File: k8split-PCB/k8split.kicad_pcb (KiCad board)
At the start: 2 copper layers, 397.3 x 124 mm, 243 parts, among them J1 AVR-ISP-6, J2 AVR-ISP-6, J3 Breakaway_Tabs, J4 Breakaway_Tabs, J5 Breakaway_Tabs, J6 Breakaway_Tabs, J7 Breakaway_Tabs, J8 Breakaway_Tabs, J9 Breakaway_Tabs, SW1 SW_Push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

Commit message: redid some silkscreen, cleaned up button move
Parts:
- removed the G*** at (257.6, 84.8)
- removed the G*** at (-2.54, 85.3)
- added G***: LOGO, cad:l, F.Cu at (119.9, 116.3)
- added G***: LOGO, cad:r, F.Cu at (158.5, 78.7)
- moved SW2 2.22 mm to (159.0, 77.2)
- moved J2 2.22 mm to (159.0, 69.6)
- moved R2 1.02 mm to (163.6, 71.1)
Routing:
- net SCK-R: track 119.8 -> 122.2 mm
- net RESET-R: track 107.7 -> 109.4 mm
- net MOSI-R: track 120.4 -> 121.4 mm
- net +5VA: track 339.9 -> 340.7 mm
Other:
- outline, holes or cut-outs redrawn

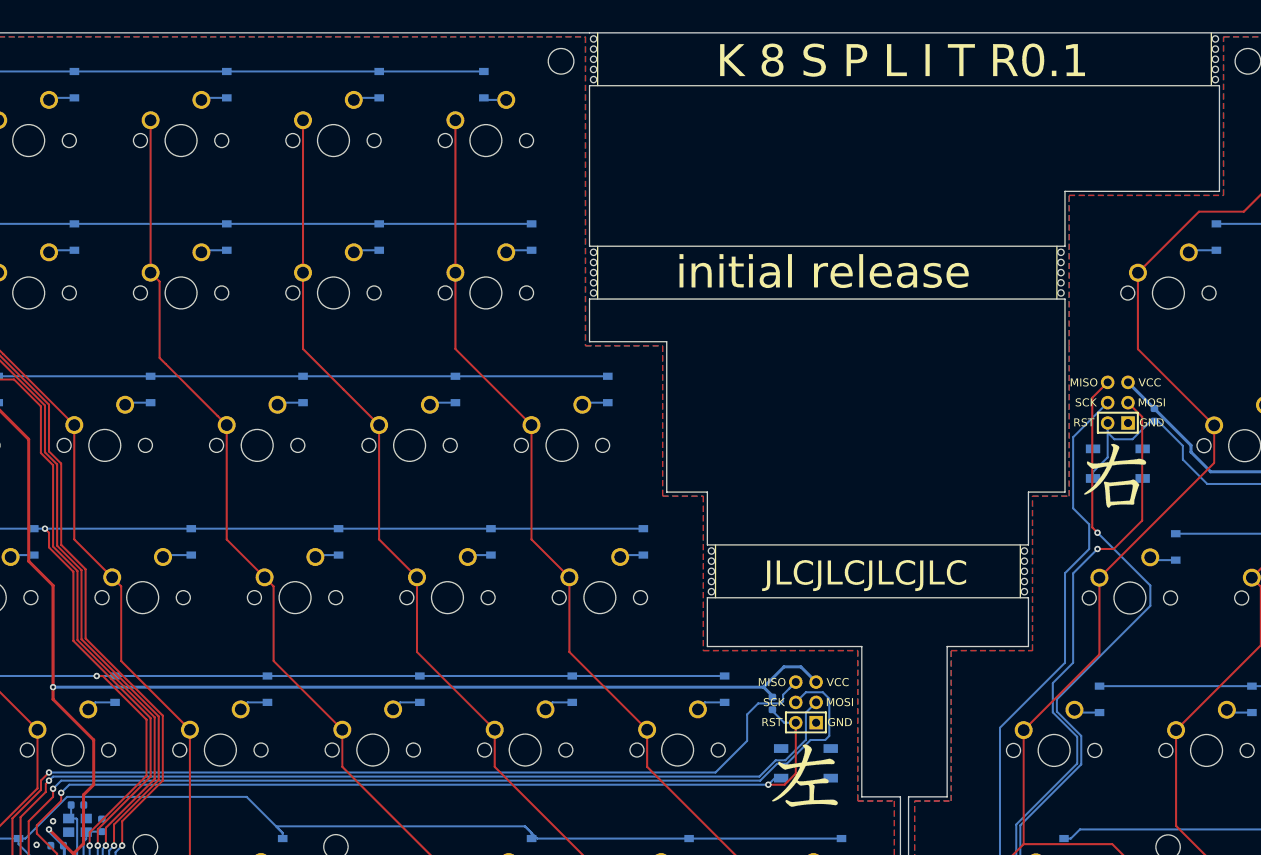
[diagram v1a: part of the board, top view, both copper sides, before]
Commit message: move silk on avr connectors
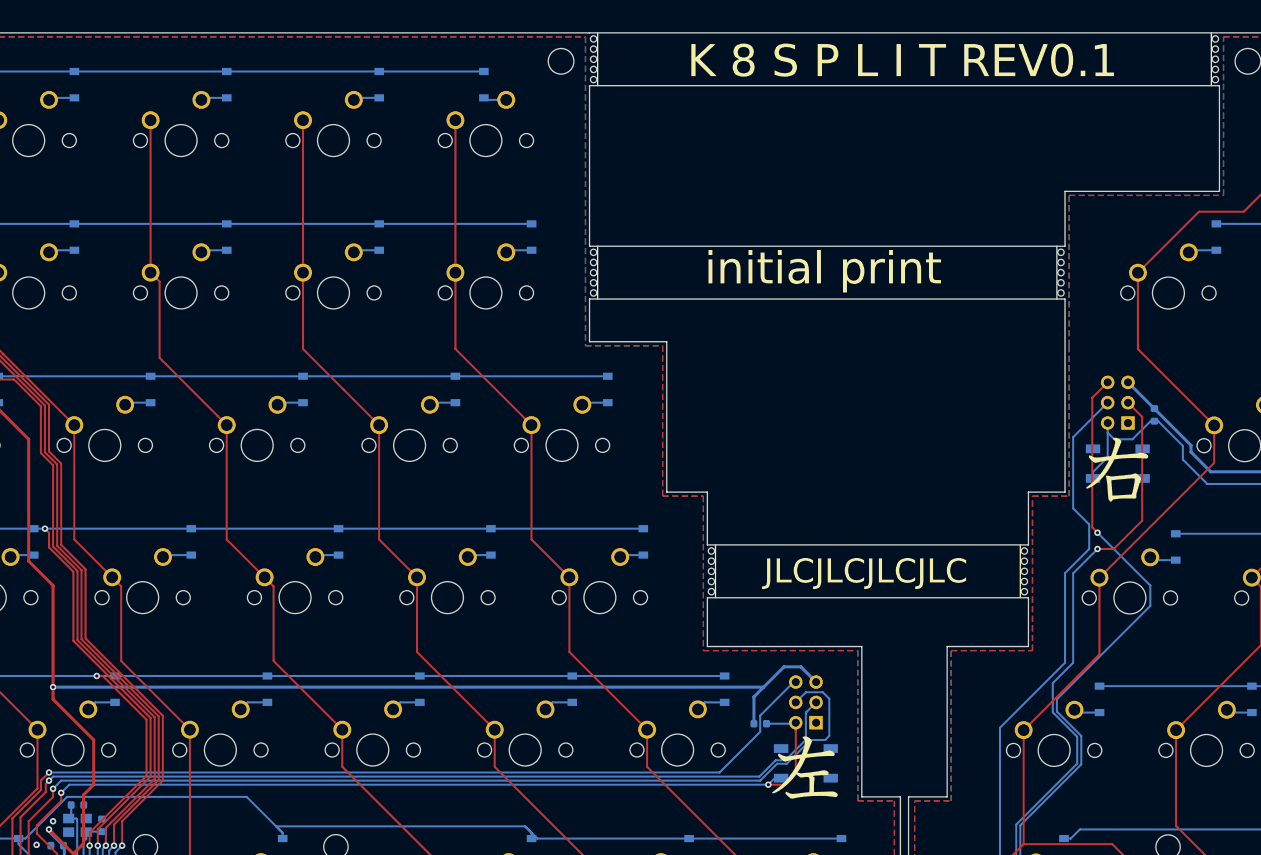
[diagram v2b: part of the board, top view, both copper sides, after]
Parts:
- moved R1 2.96 mm to (114.3, 109.7), turned to 180 degrees
- moved G*** 1.02 mm to (119.9, 115.3)
- moved G*** 0.80 mm to (158.8, 78.0)
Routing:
- net +5V: track 327.4 -> 331.0 mm
- net MISO: track 120.1 -> 117.7 mm
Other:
- board text added: "K 8 S P L I T REV0.1"
- board text added: "initial print"
- board text removed: "K 8 S P L I T R0.1"
- board text removed: "initial release"

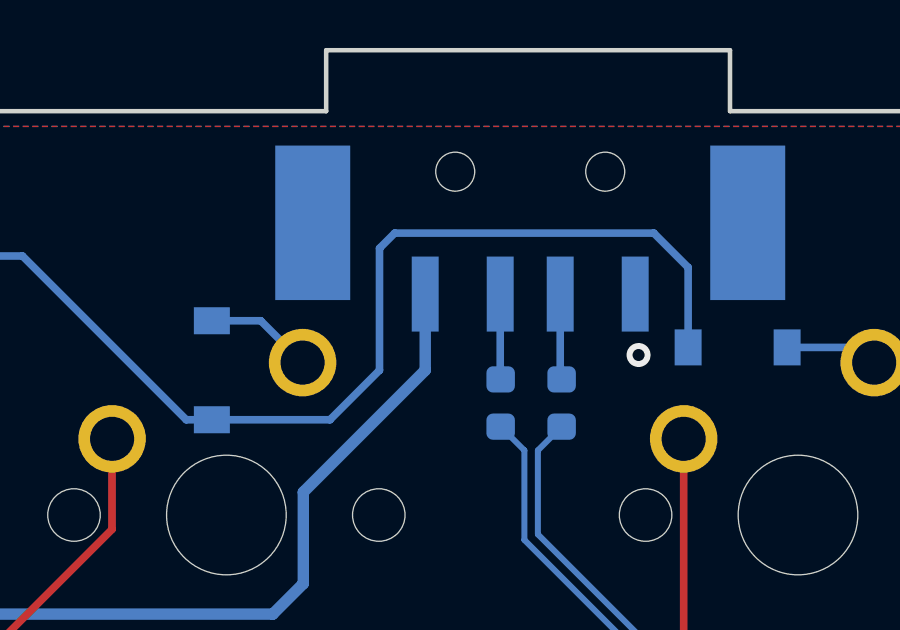
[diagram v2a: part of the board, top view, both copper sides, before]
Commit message: add silk for usb pins very uuseful
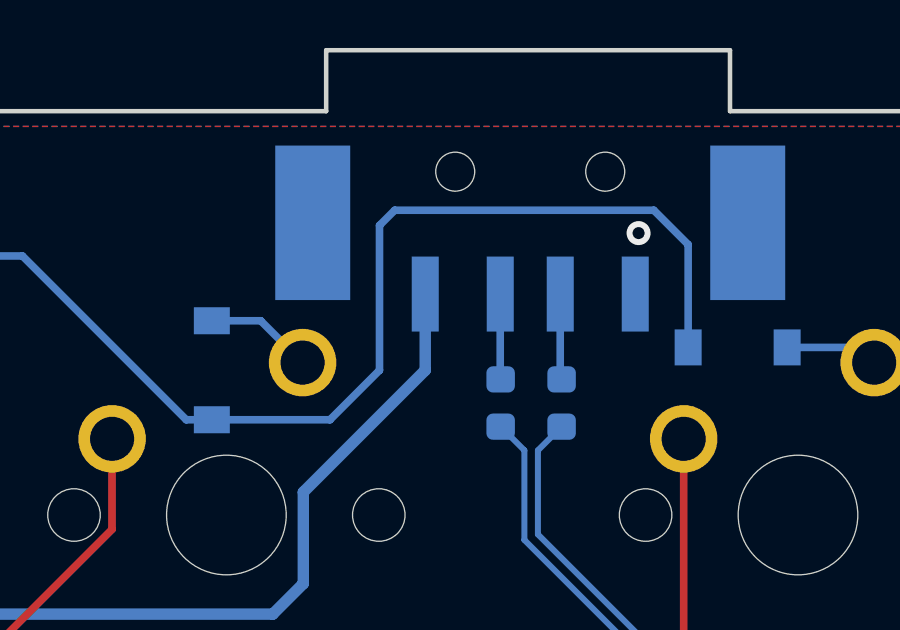
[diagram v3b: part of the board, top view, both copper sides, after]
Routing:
- net ROW0-R: track 249.0 -> 250.5 mm
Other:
- board text added: "5V"
- board text added: "D+"
- board text added: "D-"
- board text added: "GND"
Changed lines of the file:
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@@
   (general
     (thickness 1.6)
-    (drawings 58)
+    (drawings 66)
     (tracks 1146)
     (zones 0)
@@
     )
   )
+  (gr_text D+ (at -42.799 31.3182) (layer B.SilkS)
+    (effects (font (size 0.5 0.5) (thickness 0.125)) (justify mirror))
+  )
+  (gr_text 5V (at -47.244 31.496) (layer B.SilkS)
+    (effects (font (size 0.5 0.5) (thickness 0.125)) (justify mirror))
+  )
+  (gr_text D- (at -44.831 31.3182) (layer B.SilkS)
+    (effects (font (size 0.5 0.5) (thickness 0.125)) (justify mirror))
+  )
+  (gr_text GND (at -40.259 31.496) (layer B.SilkS)
+    (effects (font (size 0.5 0.5) (thickness 0.125)) (justify mirror))
+  )
+  (gr_text 5V (at 305.308 31.496) (layer B.SilkS)
+    (effects (font (size 0.5 0.5) (thickness 0.125)) (justify mirror))
+  )
+  (gr_text D- (at 307.721 31.3182) (layer B.SilkS)
+    (effects (font (size 0.5 0.5) (thickness 0.125)) (justify mirror))
+  )
+  (gr_text D+ (at 309.753 31.3182) (layer B.SilkS)
+    (effects (font (size 0.5 0.5) (thickness 0.125)) (justify mirror))
+  )
+  (gr_text GND (at 312.293 31.496) (layer B.SilkS)
+    (effects (font (size 0.5 0.5) (thickness 0.125)) (justify mirror))
+  )
   (dimension 123.952 (width 0.15) (layer Dwgs.User)
     (gr_text "123.952 mm" (at 342.422 83.312 90) (layer Dwgs.User)
@@
   (segment (start 301.118 28.195) (end 301.88281 28.95981) (width 0.254) (layer B.Cu) (net 6) (status 30))
   (segment (start 187.452 132.3595) (end 187.6805 132.588) (width 0.381) (layer B.Cu) (net 6) (status 30))
-  (via (at 312.42 31.496) (size 0.8) (drill 0.4) (layers F.Cu B.Cu) (net 6))
+  (via (at 312.42 27.432) (size 0.8) (drill 0.4) (layers F.Cu B.Cu) (net 6))
   (segment (start 199.923 139.6495) (end 199.3645 140.208) (width 0.381) (layer B.Cu) (net 6) (status 20))
   (segment (start 199.923 138.415) (end 199.923 139.6495) (width 0.381) (layer B.Cu) (net 6) (status 10))
@@
   (segment (start 285.623 28.195) (end 220.217 28.195) (width 0.254) (layer B.Cu) (net 66) (status 10))
   (segment (start 314.13 31.242) (end 313.944 31.056) (width 0.254) (layer B.Cu) (net 66) (status 30))
-  (segment (start 302.134 33.654) (end 298.196 33.654) (width 0.254) (layer B.Cu) (net 66) (status 20))
-  (segment (start 303.784 32.004) (end 302.134 33.654) (width 0.254) (layer B.Cu) (net 66))
-  (segment (start 314.072 28.576) (end 312.928 27.432) (width 0.254) (layer B.Cu) (net 66))
-  (segment (start 312.928 27.432) (end 304.292 27.432) (width 0.254) (layer B.Cu) (net 66))
-  (segment (start 314.072 31.242) (end 314.072 28.576) (width 0.254) (layer B.Cu) (net 66) (status 10))
-  (segment (start 304.292 27.432) (end 303.784 27.94) (width 0.254) (layer B.Cu) (net 66))
-  (segment (start 303.784 27.94) (end 303.784 32.004) (width 0.254) (layer B.Cu) (net 66))
   (segment (start 196.596 113.792) (end 194.056 116.332) (width 0.254) (layer B.Cu) (net 66))
   (segment (start 194.056 116.332) (end 194.056 117.856) (width 0.254) (layer F.Cu) (net 66))
@@
   (segment (start 191.116001 126.092001) (end 191.516 126.492) (width 0.254) (layer F.Cu) (net 66))
   (segment (start 194.056 117.856) (end 191.116001 120.795999) (width 0.254) (layer F.Cu) (net 66))
+  (segment (start 312.928 26.67) (end 314.072 27.814) (width 0.254) (layer B.Cu) (net 66))
+  (segment (start 302.134 33.654) (end 303.784 32.004) (width 0.254) (layer B.Cu) (net 66))
+  (segment (start 298.196 33.654) (end 302.134 33.654) (width 0.254) (layer B.Cu) (net 66))
+  (segment (start 303.784 32.004) (end 303.784 27.178) (width 0.254) (layer B.Cu) (net 66))
+  (segment (start 303.784 27.178) (end 304.292 26.67) (width 0.254) (layer B.Cu) (net 66))
+  (segment (start 304.292 26.67) (end 312.928 26.67) (width 0.254) (layer B.Cu) (net 66))
+  (segment (start 314.072 27.814) (end 314.072 31.242) (width 0.254) (layer B.Cu) (net 66))
   (segment (start 168.131333 50.545) (end 167.865888 50.810445) (width 0.254) (layer B.Cu) (net 67) (status 30))
   (segment (start 171.323 50.545) (end 168.131333 50.545) (width 0.254) (layer B.Cu) (net 67) (status 30))

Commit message: avr program header typesetting wwow
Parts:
- moved R2 2.43 mm to (165.4, 72.8)
- moved R1 1.65 mm to (112.6, 109.7)
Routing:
- net COL1-R: track 165.7 -> 159.4 mm
- net COL0-R: track 182.7 -> 185.5 mm
- net RESET-R: track 109.4 -> 107.8 mm
- net MISO: track 117.7 -> 118.8 mm
- net +5V: track 331.0 -> 331.6 mm

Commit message: add some corona jokes
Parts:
- added G***: LOGO, cad:corona, B.Cu at (128.5, 121.9)
- added G***: LOGO, cad:corona, B.Cu at (136.1, 121.9)
- moved D48 6.10 mm to (118.4, 125.7)
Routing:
- net ROW5: track 181.9 -> 176.5 mm
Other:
- board text added: "might contain corona proceed with caution"

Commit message: trace cleanup
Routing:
- net COL5-R: track 211.8 -> 205.3 mm
- net MISO-R: track 125.0 -> 118.7 mm
- net SCK-R: track 122.2 -> 117.7 mm
- net +5V: track 331.6 -> 334.5 mm
- net ROW2: track 212.1 -> 210.0 mm
- net MOSI-R: track 121.4 -> 119.5 mm
- net +5VA: track 340.7 -> 342.6 mm
- net COL3-R: track 170.5 -> 169.4 mm
- net MOSI: track 118.3 -> 119.4 mm
- net ROW5-R: track 195.3 -> 194.4 mm
- net Net-(D96-Pad2): track 3.75 -> 2.97 mm
- net RESET: track 120.6 -> 120.0 mm
- net SCK: track 125.5 -> 124.9 mm
